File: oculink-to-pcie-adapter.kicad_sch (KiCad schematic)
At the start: 5 parts, among them J6 Molex_Mini-Fit-Jr_2x4_39-28-8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

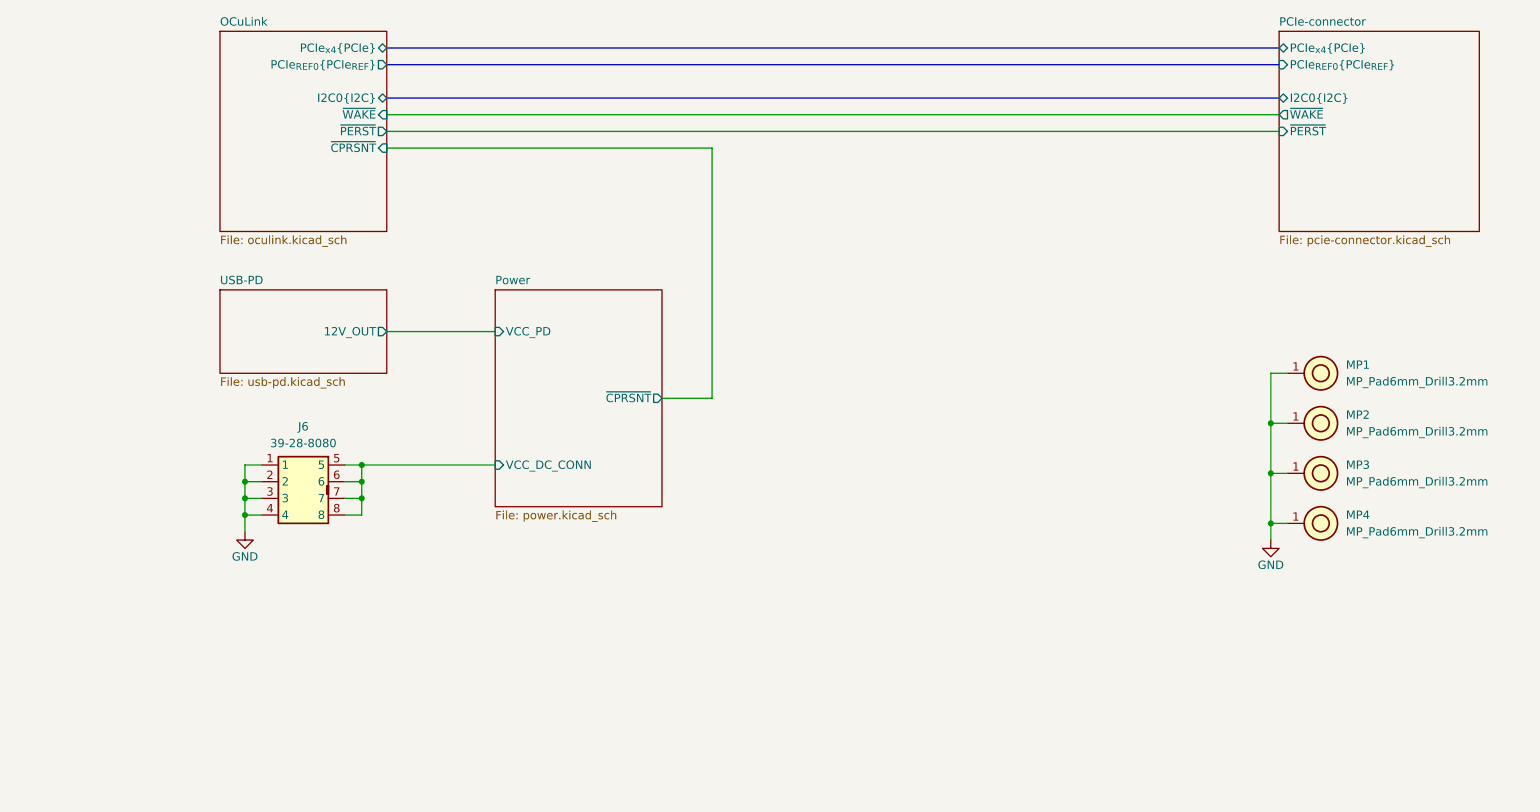
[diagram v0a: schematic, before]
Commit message: [#79426] Removed power sequencing, added PERST control
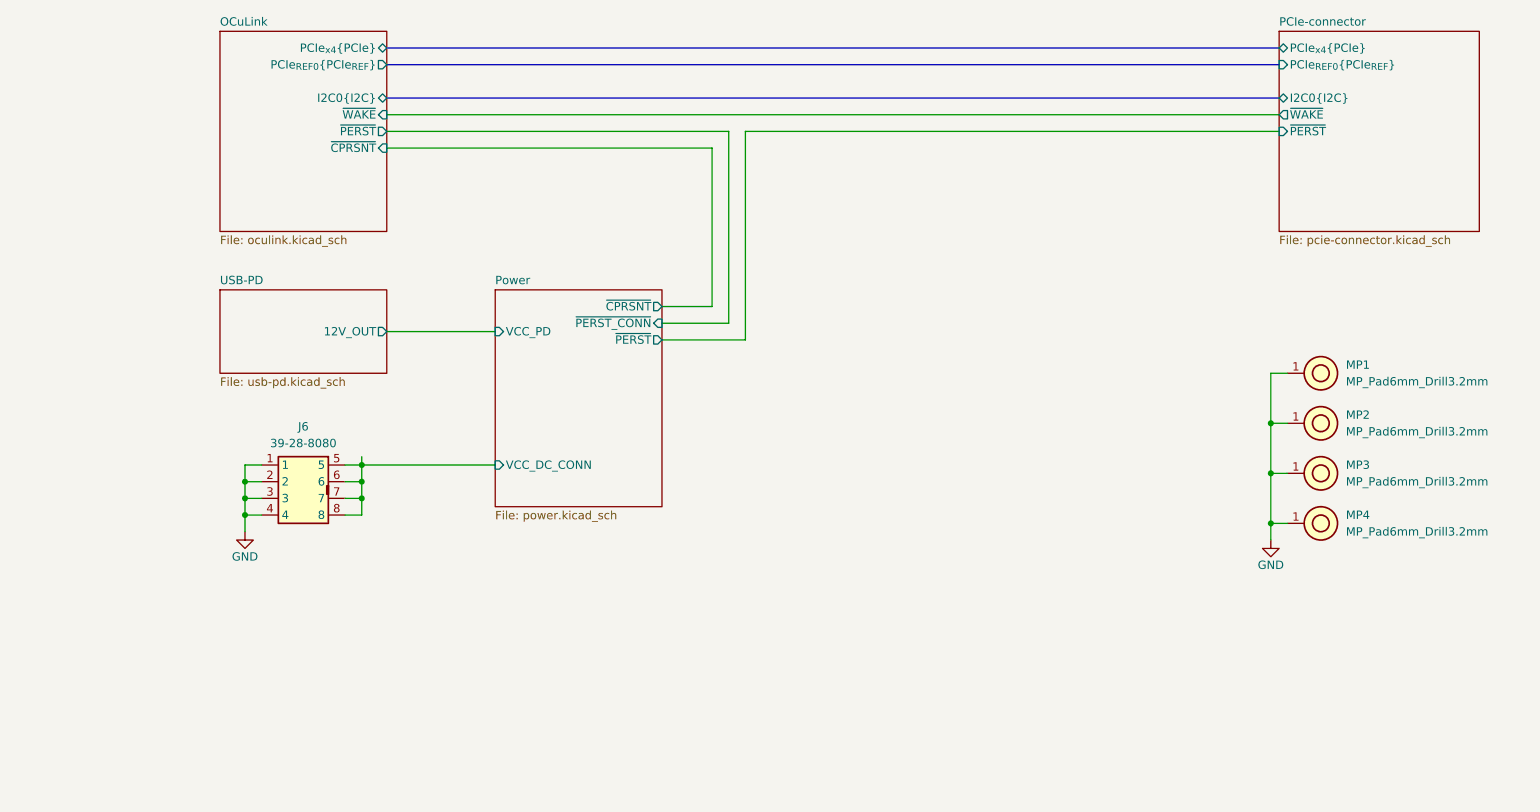
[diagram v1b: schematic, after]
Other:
- sheet Power ports: added ~{PERST_CONN}, ~{PERST}; removed none
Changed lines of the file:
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@@
 	(wire
 		(pts
-			(xy 137.16 130.81) (xy 273.05 130.81)
+			(xy 137.16 130.81) (xy 189.23 130.81)
+		)
+		(stroke
+			(width 0)
+			(type default)
+		)
+	)
+	(wire
+		(pts
+			(xy 179.07 162.56) (xy 191.77 162.56)
 		)
 		(stroke
@@
 	(wire
 		(pts
+			(xy 191.77 162.56) (xy 191.77 130.81)
+		)
+		(stroke
+			(width 0)
+			(type default)
+		)
+	)
+	(wire
+		(pts
 			(xy 137.16 128.27) (xy 273.05 128.27)
 		)
@@
 	(wire
 		(pts
+			(xy 189.23 160.02) (xy 179.07 160.02)
+		)
+		(stroke
+			(width 0)
+			(type default)
+		)
+	)
+	(wire
+		(pts
+			(xy 191.77 130.81) (xy 273.05 130.81)
+		)
+		(stroke
+			(width 0)
+			(type default)
+		)
+	)
+	(wire
+		(pts
 			(xy 271.78 182.88) (xy 274.32 182.88)
 		)
@@
 	(wire
 		(pts
+			(xy 189.23 130.81) (xy 189.23 160.02)
+		)
+		(stroke
+			(width 0)
+			(type default)
+		)
+	)
+	(wire
+		(pts
+			(xy 133.35 180.34) (xy 133.35 181.61)
+		)
+		(stroke
+			(width 0)
+			(type default)
+		)
+	)
+	(wire
+		(pts
 			(xy 133.35 186.69) (xy 133.35 189.23)
 		)
@@
 	(wire
 		(pts
-			(xy 179.07 171.45) (xy 186.69 171.45)
+			(xy 179.07 157.48) (xy 186.69 157.48)
 		)
 		(stroke
@@
 	(wire
 		(pts
-			(xy 186.69 171.45) (xy 186.69 133.35)
+			(xy 186.69 157.48) (xy 186.69 133.35)
 		)
 		(stroke
@@
 			(width 0)
 			(type default)
+		)
+	)
+	(netclass_flag ""
+		(length 2.54)
+		(shape round)
+		(at 133.35 180.34 0)
+		(effects
+			(font
+				(size 1.27 1.27)
+				(color 255 0 0 1)
+			)
+			(justify left bottom)
+		)
+		(property "Netclass" "PWR"
+			(at 133.35 176.276 0)
+			(effects
+				(font
+					(size 1.27 1.27)
+				)
+			)
+		)
+		(property "Component Class" ""
+			(at -240.03 135.89 0)
+			(effects
+				(font
+					(size 1.27 1.27)
+					(italic yes)
+				)
+			)
 		)
 	)
@@
 		)
 		(pin "~{CPRSNT}" output
-			(at 179.07 171.45 0)
+			(at 179.07 157.48 0)
 			(effects
 				(font
@@
 			)
 		)
+		(pin "~{PERST_CONN}" input
+			(at 179.07 160.02 0)
+			(effects
+				(font
+					(size 1.27 1.27)
+				)
+				(justify right)
+			)
+		)
+		(pin "~{PERST}" output
+			(at 179.07 162.56 0)
+			(effects
+				(font
+					(size 1.27 1.27)
+				)
+				(justify right)
+			)
+		)

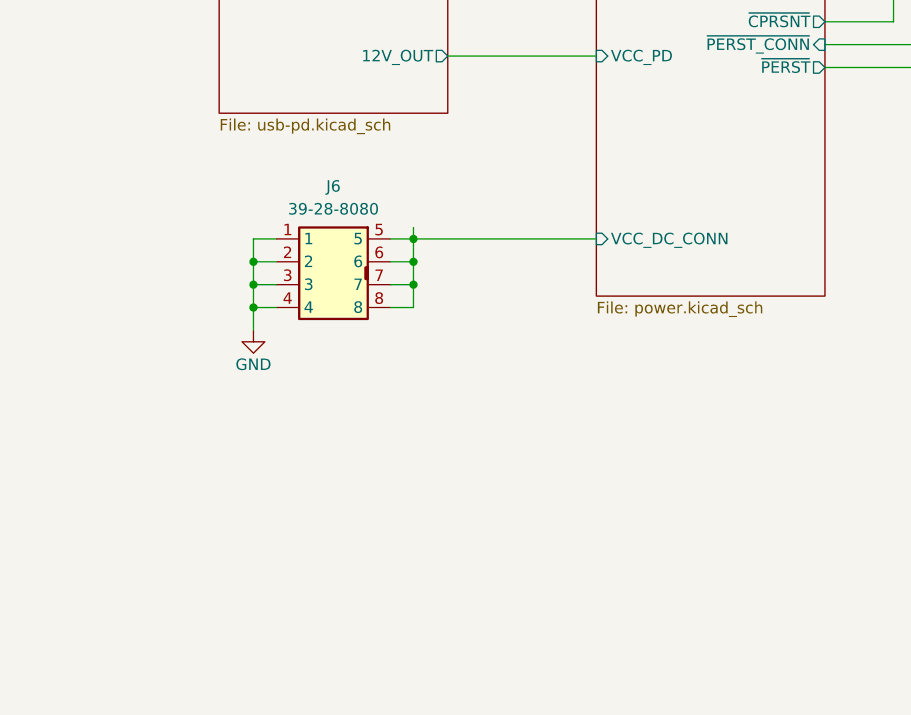
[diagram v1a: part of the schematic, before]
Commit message: [#79426] Add PCIe power connector
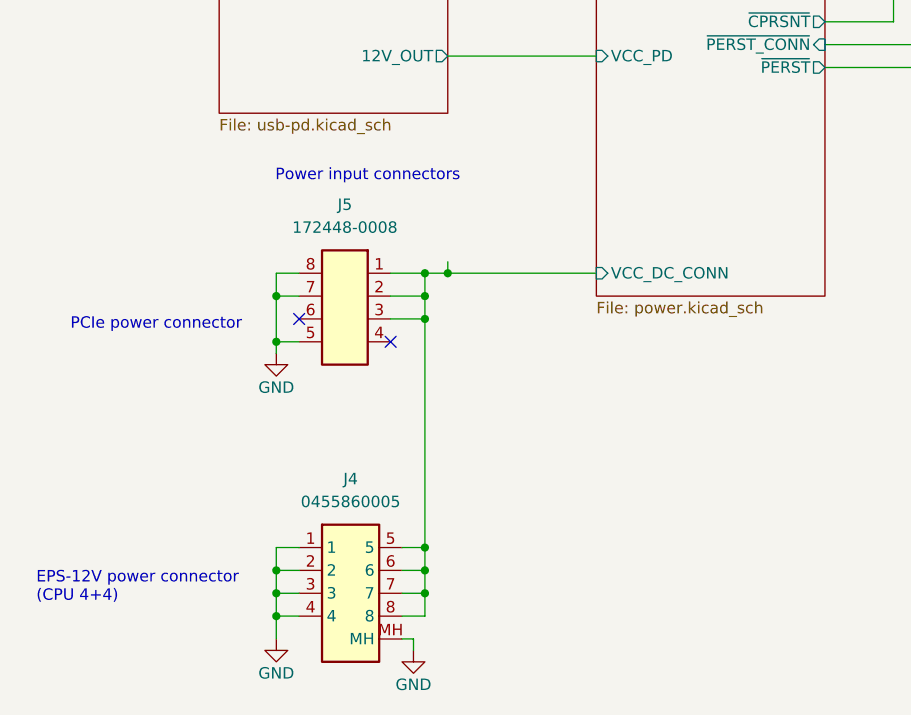
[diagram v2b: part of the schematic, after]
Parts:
- removed J6: Molex_Mini-Fit-Jr_2x4_39-28-8080, antmicro-footprints:MOLEX_39288080, symbol antmicroWire2BoardConnectors:Molex_Mini-Fit-Jr_2x4_39-28-8080
- added J4: Molex_Mini-Fit-Jr_2x4_0455860005, antmicro-footprints:Molex_Mini-Fit-Jr_2x4_0455860005, symbol antmicroWire2BoardConnectors:Molex_Mini-Fit-Jr_2x4_0455860005
- added J5: Molex_Mini-Fit_2x4_172448-0008_Horizontal, antmicro-footprints:Molex_Mini-Fit_2x4_172448-0008_Horizontal, symbol antmicroWire2BoardConnectors:Molex_Mini-Fit_2x4_172448-0008_Horizontal
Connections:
- net GND: now also J4.1, J4.2, J4.3, J4.4, J4.MH, J5.5, J5.7, J5.8
- net Power/VCC_DC_CONN: now also J4.5, J4.6, J4.7, J4.8, J5.1, J5.2, J5.3
- no-connect marks 0 -> 2
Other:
- note added: "EPS-12V power connector (CPU 4+4)"
- note added: "PCIe power connector"
- note added: "Power input connectors"

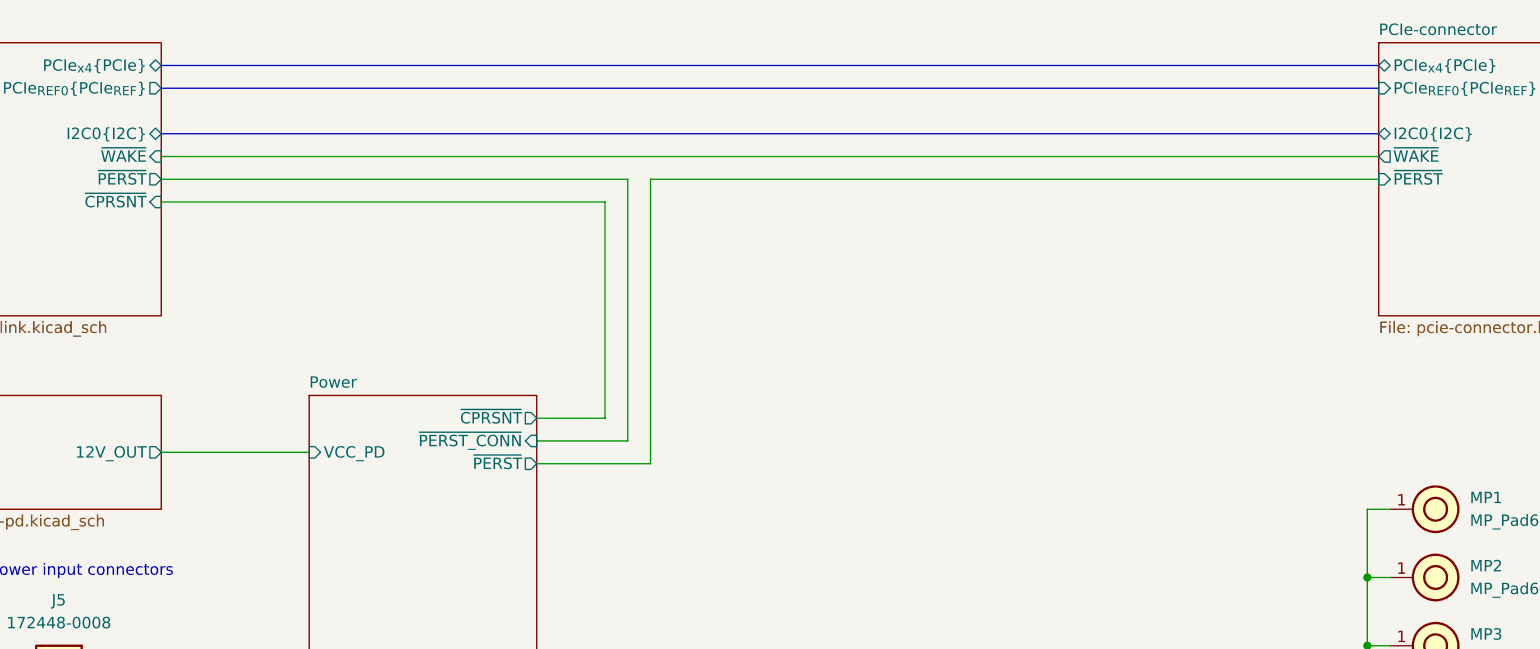
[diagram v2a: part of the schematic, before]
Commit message: [#79426] Add optional clock generator
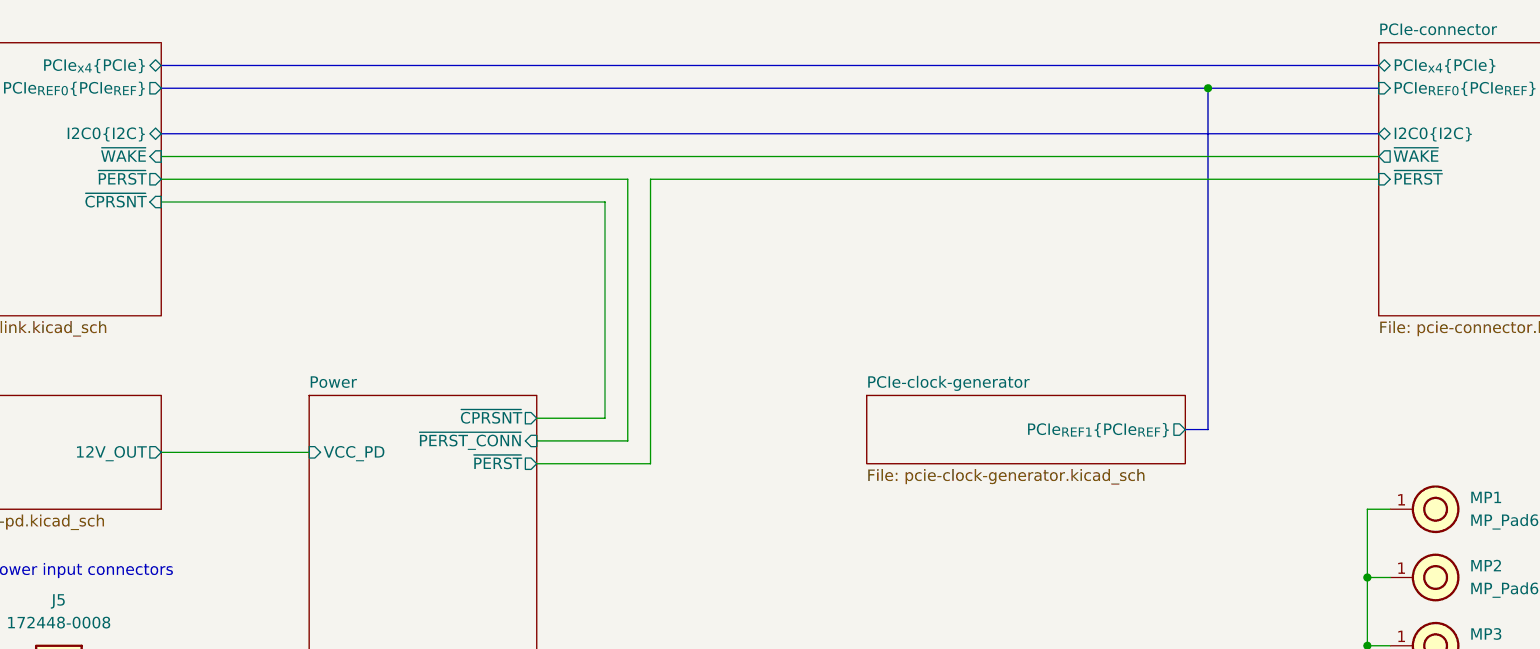
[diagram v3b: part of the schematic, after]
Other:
- added sheet PCIe-clock-generator (pcie-clock-generator.kicad_sch)
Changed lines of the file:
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@@
+	)
+	(junction
+		(at 254 120.65)
+		(diameter 0)
+		(color 0 0 0 0)
 	)
 	(junction
@@
 		)
 	)
+	(bus
+		(pts
+			(xy 254 120.65) (xy 273.05 120.65)
+		)
+		(stroke
+			(width 0)
+			(type default)
+		)
+	)
 	(wire
 		(pts
@@
 		)
 	)
+	(bus
+		(pts
+			(xy 254 158.75) (xy 254 120.65)
+		)
+		(stroke
+			(width 0)
+			(type default)
+		)
+	)
 	(wire
 		(pts
@@
 		)
 	)
+	(bus
+		(pts
+			(xy 251.46 158.75) (xy 254 158.75)
+		)
+		(stroke
+			(width 0)
+			(type default)
+		)
+	)
 	(wire
 		(pts
@@
 	(bus
 		(pts
-			(xy 137.16 120.65) (xy 273.05 120.65)
+			(xy 137.16 120.65) (xy 254 120.65)
 		)
 		(stroke
@@
 				)
 			)
+		)
+	)
+	(sheet
+		(at 215.9 154.94)
+		(size 35.56 7.62)
+		(exclude_from_sim no)
+		(in_bom no)
+		(on_board yes)
+		(dnp yes)
+		(fields_autoplaced yes)
+		(stroke
+			(width 0.1524)
+			(type solid)
+		)
+		(fill
+			(color 0 0 0 0.0000)
+		)
+		(property "Sheetname" "PCIe-clock-generator"
+			(at 215.9 154.2284 0)
+			(effects
+				(font
+					(size 1.27 1.27)
+				)
+				(justify left bottom)
+			)
+		)
+		(property "Sheetfile" "pcie-clock-generator.kicad_sch"
+			(at 215.9 163.1446 0)
+			(effects
+				(font
+					(size 1.27 1.27)
+				)
+				(justify left top)
+			)
+		)
+		(pin "PCIe_{REF1}{PCIe_{REF}}" output
+			(at 251.46 158.75 0)
+			(effects
+				(font
+					(size 1.27 1.27)
+				)
+				(justify right)
+			)
+		)
+		(instances
+			(project "oculink-to-pcie-adapter"
+				(path "/44c3be85-0a18-4d93-a9a5-650ee09b6032"
+					(page "8")
+				)
+			)

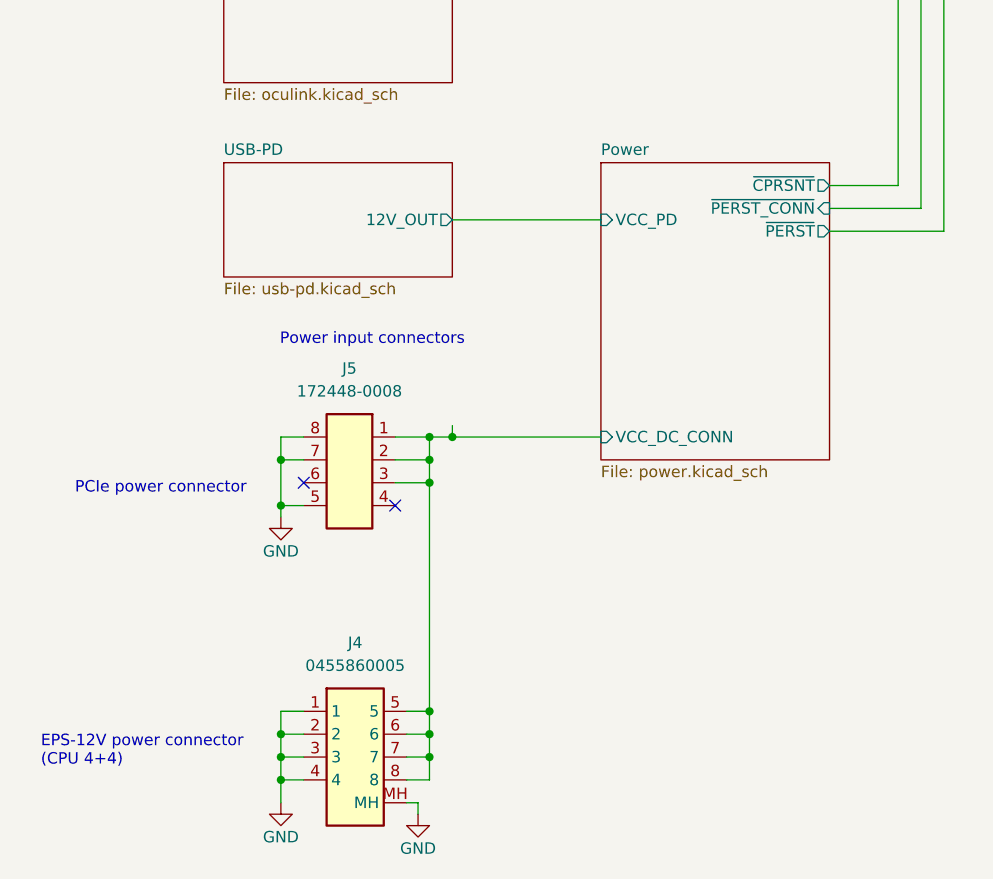
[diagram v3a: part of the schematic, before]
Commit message: [#79426] Connect DC input connectors via ideal diodes, change 15V TVS to 12V TVS
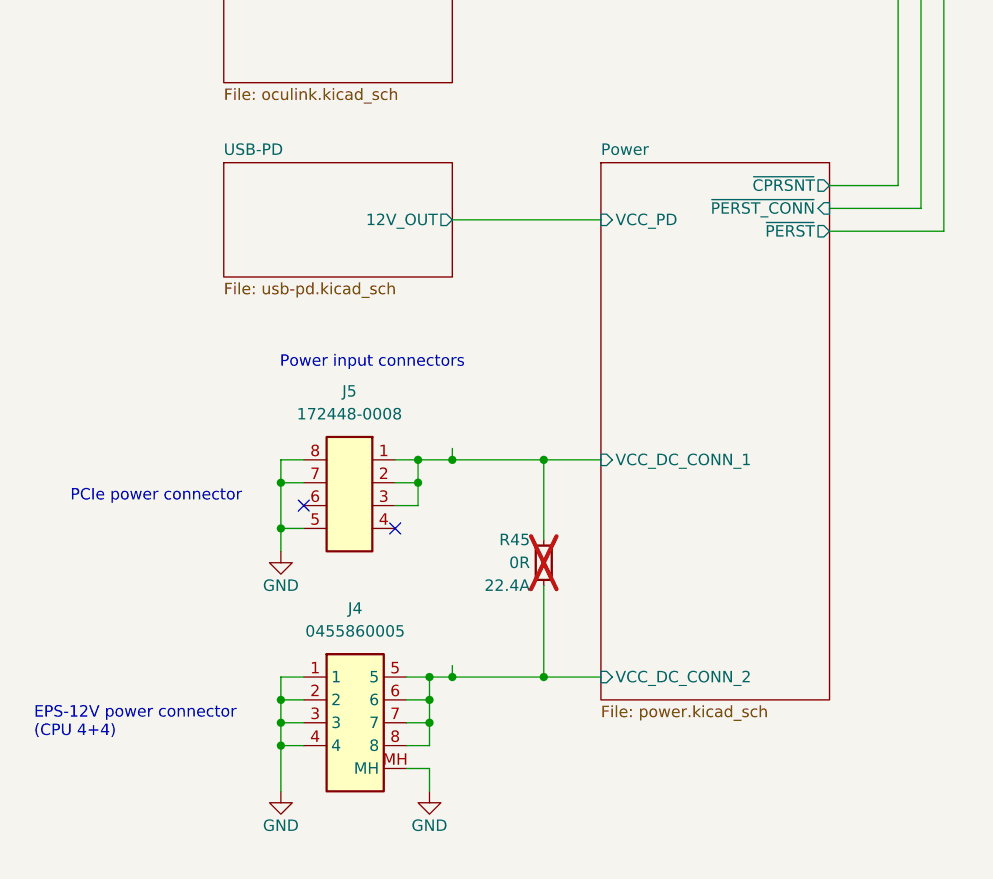
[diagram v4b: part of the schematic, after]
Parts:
- added R45: R_0R_22.4A_0603, antmicro-footprints:R_0603_1608Metric, symbol antmicroResistors0603:R_0R_22.4A_0603
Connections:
- net Power/VCC_DC_CONN renamed Power/VCC_DC_CONN_2
- net Power/VCC_DC_CONN_2: now also R45.1; no longer J5.1, J5.2, J5.3
- new net Power/VCC_DC_CONN_1: J5.1, J5.2, J5.3, R45.2
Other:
- sheet Power ports: added VCC_DC_CONN_1, VCC_DC_CONN_2; removed VCC_DC_CONN
- moved on the sheet: J4, J5
